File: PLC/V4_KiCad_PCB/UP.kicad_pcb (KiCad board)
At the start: 2 copper layers, 208 x 80 mm, 251 parts, among them J18 01x03_Male, J19 01x08_Male, J20 01x02_Male, J21 02x02_Male, J22 opt. Connector, J23 opt. Connector, J24 01x05_Male, J26 01x04, J29 Lötauge, J30 Lötauge, J31 Lötauge, J32 Lötauge, J34 Brücke, J35 Lötauge, J36 Brücke, J38 Lötauge, J39 Lötauge, J49 01x15 Male zu OP, J50 01x15 Male zu OP, J53 Lötauge, J54 Lötauge, J55 Lötauge, J56 Lötauge, J57 Lötauge, J58 Lötauge, J59 Lötauge, J60 Lötauge, J63 Lötauge, J64 Lötauge, J65 Lötauge, J66 Flachstecker, Q2 IRLML 2244, U11 2S7WA_2405_S3RP, U12 2S7WA_2405_S3RP, U13 LT1086 3.3, U14 MCP23S17, U15 LTV-844, U16 LTV-844, U17 LTV-844, U18 LTV-844, U19 BSP-452, U20 BSP-452, U21 BSP-452, U22 BSP-452, U23 BSP-452, U24 BSP-452, U25 BSP-452, U26 BSP-452, U27 BSP-452, U28 BSP-452, U29 BSP-452, U30 BSP-452, U31 BSP-452, U32 BSP-452, U33 BSP-452, U34 BSP-452, U35 ADuM1401xRW, U37 LT1086 3.3, U38 MCP4922, U41 LT 1078, U44 2S7WB_2415S3RP, U45 ADR03ARZ, U46 LCN78_05-0.5

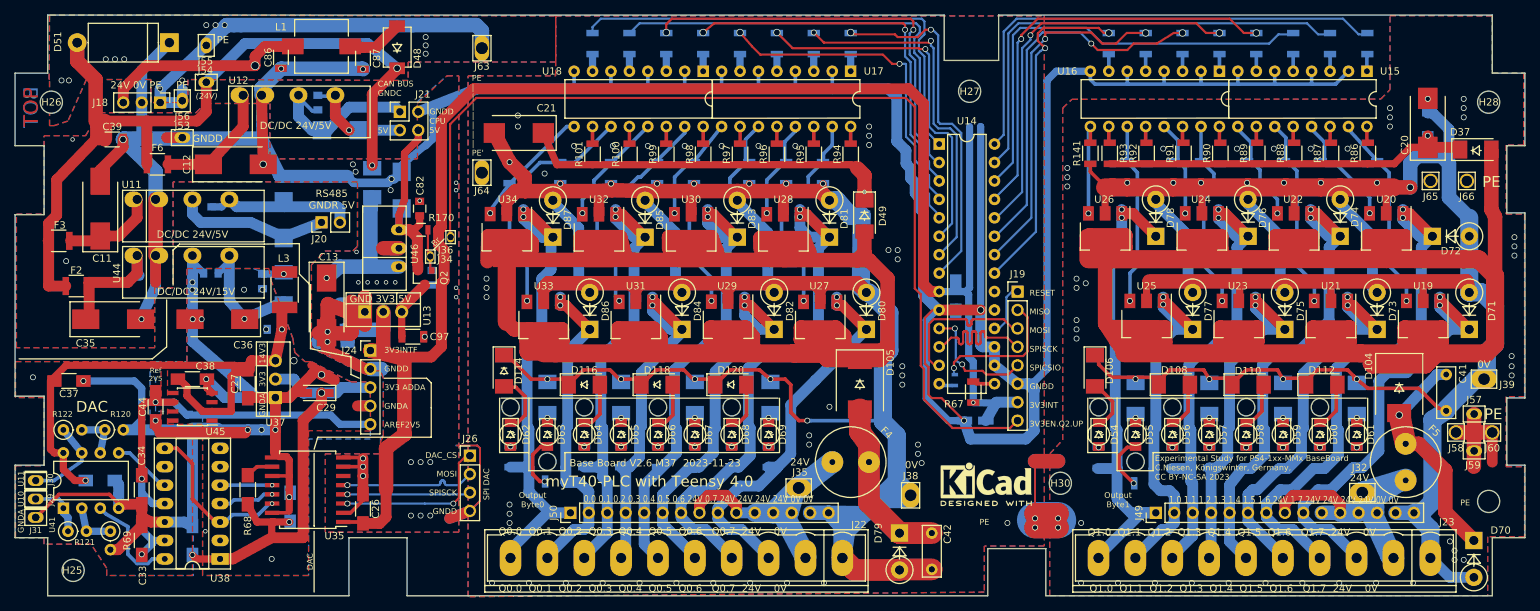
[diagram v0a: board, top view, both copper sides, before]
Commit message: Ansteuerung Q2 verändert
Ansteuerung auf UP über Brücke J34 J36 ist entfallen.
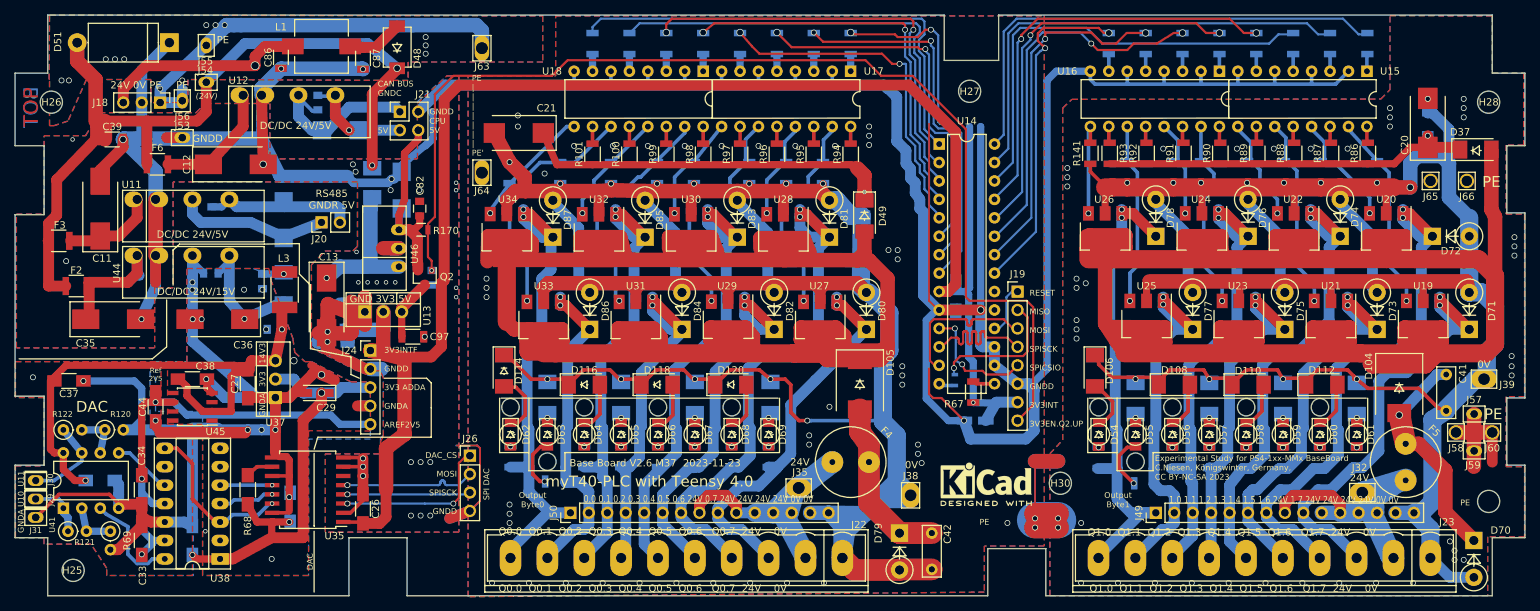
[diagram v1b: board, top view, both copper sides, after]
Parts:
- removed J34, J36: Brücke, mylib:Lötauge-Junction_1x1.5-0.8
- J26: value 01x04 -> 01x04_Male
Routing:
- net GNDD: track 567.2 -> 584.9 mm
- net /COLDSTART_3V3INT: track 145.2 -> 153.7 mm, vias 3 -> 2
- net +3V3: track 242.4 -> 245.9 mm
- net /PE: vias 111 -> 112
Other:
- board text removed: "Br"

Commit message: Kaltstart Überarbeitung
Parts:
- added C98: 100n, Capacitors_SMD:C_1206, F.Cu at (189.0, 73.8)
- added D50: BZX84C-3V6, Diodes_SMD:D_SOT-23_ANK, B.Cu at (106.1, 86.9)
- added R50: 10k, Resistors_SMD:R_0805, F.Cu at (189.7, 66.5)
- added U40: ADM-803R, TO_SOT_Packages_SMD:SOT-23, F.Cu at (189.5, 69.6)
- C96: moved to F.Cu
- C97: moved to B.Cu
- U46: value LCN78_05-0.5 -> LCN78_05-1.0
- moved R170 17.3 mm to (106.1, 86.9)
- moved C14 10.7 mm to (105.1, 83.8), turned to 0 degrees
- moved Q2 9.87 mm to (102.6, 85.3)
- moved C96 8.15 mm to (106.2, 84.2), turned to 0 degrees
- moved C97 7.19 mm to (100.6, 78.5), turned to 180 degrees
- moved C15 4.74 mm to (100.0, 83.2), turned to 180 degrees
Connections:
- net /COLDSTART_3V3INT renamed /3V3EN_Q2_UP
- C18 pad 2: +3V3 -> /3V3_INT
- C19 pad 1: +3V3 -> /3V3_INT
- C26 pad 2: +3V3 -> /3V3_INT
- C97 pad 1: Net-(C97-Pad1) -> /5V_CPU
- J19 pad 7: +3V3 -> /3V3_INT
- J24 pad 1: +3V3 -> /3V3_INT
- Q2 pad 2: /5V_CPU -> +3V3
- Q2 pad 3: Net-(C97-Pad1) -> /3V3_INT
- R170 pad 2: /5V_CPU -> +3V3
- R67 pad 1: +3V3 -> /3V3_INT
- U13 pad 3: Net-(C97-Pad1) -> /5V_CPU
- U14 pad 9: +3V3 -> /3V3_INT
- U35 pad 1: +3V3 -> /3V3_INT
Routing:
- net /3V3_INT: track 0.00 -> 231.5 mm, vias 0 -> 3
- net +3V3: track 245.9 -> 151.0 mm, vias 4 -> 2
- net /3V3EN_Q2_UP: track 153.7 -> 168.4 mm, vias 2 -> 1
- net /~RESET: track 7.21 -> 19.9 mm, vias 0 -> 1
- net /5V_CPU: track 27.4 -> 37.3 mm, vias 2 -> 3
- net Net-(C97-Pad1): track 8.45 -> 0.00 mm, vias 1 -> 0
- net GNDD: track 584.9 -> 588.5 mm, vias 46 -> 50
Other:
- board text added: "3V3 ADDA GNDA AREF2V5"
- board text added: "3V3INT GNDD"
- board text added: "3V3INT GNDD 3V3 ADDA GNDA AREF2V5"
- board text added: "Interfaces 5V.3V3.GND"
- board text removed: "3V3INTF GNDD 3V3 ADDA GNDA AREF2V5"
- board text removed: "Interfaces 5V 3V3 GND"

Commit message: V2.6 R38 final PFS
M38 final Version for PFS variant
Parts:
- removed D50: BZX84C-3V6, Diodes_SMD:D_SOT-23_ANK
- added U51: SN74LV1T08, TO_SOT_Packages_SMD:SOT-23-5, B.Cu at (106.8, 80.5)
- C96: moved to B.Cu
- moved C96 35.1 mm to (108.3, 49.3), turned to 225 degrees
- moved R170 1.59 mm to (106.0, 85.3), turned to 270 degrees
- moved J63 0.76 mm to (113.6, 44.6)
- moved J64 0.76 mm to (113.6, 61.7)
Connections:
- Q2 pad 1: /3V3EN_Q2_UP -> Net-(Q2-Pad1)
- R170 pad 1: /3V3EN_Q2_UP -> Net-(Q2-Pad1)
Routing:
- net /3V3EN_Q2_UP: track 168.4 -> 159.0 mm, vias 1 -> 3
- net Net-(Q2-Pad1): track 0.00 -> 5.60 mm, vias 0 -> 1
- net GNDD: track 588.5 -> 585.6 mm, vias 50 -> 49
- net +3V3: track 151.0 -> 152.7 mm, vias 2 -> 3
- net /PE: track 106.1 -> 104.8 mm
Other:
- board text added: "Base Board V2.6 M38 2024-01-17"
- board text added: "FFC/PFS Base Board V2.6 M38 2024-01-17"
- board text removed: "Base Board V2.6 M37 2023-11-23"
- board text removed: "FFC/PFS Base Board V2.6 M37 2023-11-23"

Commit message: V2.8 M40 Coldstart Issues
Coldstart issues, some PullUps to high dimensioned, no high logic resulting together with switched-off Teensy and its input impedances.
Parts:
- R50: value 10k -> 1k
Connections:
- U51 pad 3: +3V3 -> GNDD
- U51 pad 5: GNDD -> +3V3
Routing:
- net +3V3: track 152.7 -> 155.0 mm, vias 3 -> 2
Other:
- board text added: "Base Board V2.8 M40 2024-05-27"
- board text added: "FFC/PFS Base Board V2.8 M40 2024-05-27"
- board text removed: "Base Board V2.6 M38 2024-01-17"
- board text removed: "FFC/PFS Base Board V2.6 M38 2024-01-17"

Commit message: Final version V2.9 M41
Cold start issues solved.
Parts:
- added J34: 01x01_Male, Connector_PinHeader_2.54mm:PinHeader_1x01_P2.54mm_Vertical, F.Cu at (105.5, 58.4)
- D51: value 1.5KE30CA -> 1.5KE27CA
- R50: value 1k -> 220
- moved D51 12.7 mm to (58.6, 43.8), turned to 0 degrees
- moved C39 1.83 mm to (64.9, 56.1), turned to 270 degrees
- moved C85 0.13 mm to (91.6, 52.1)
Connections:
- D51 pad 1: GNDD -> Net-(C39-Pad1)
- D51 pad 2: Net-(C39-Pad1) -> GNDD
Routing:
- net GNDD: track 585.6 -> 577.3 mm, vias 49 -> 53
- net Net-(C39-Pad1): track 112.5 -> 110.5 mm
- net +3V3: track 155.0 -> 156.6 mm, vias 2 -> 3
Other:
- board text added: "Base Board V2.9 M41 2024-06-09"
- board text added: "FFC/PFS Base Board V2.9 M41 2024-06-09"
- board text added: "GNDD CPU 5V 3V3"
- board text removed: "Base Board V2.8 M40 2024-05-27"
- board text removed: "FFC/PFS Base Board V2.8 M40 2024-05-27"
- board text removed: "GNDD CPU 5V"
